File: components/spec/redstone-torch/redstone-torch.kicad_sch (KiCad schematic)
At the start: 3 parts, among them Q12 Q_NMOS_DGS

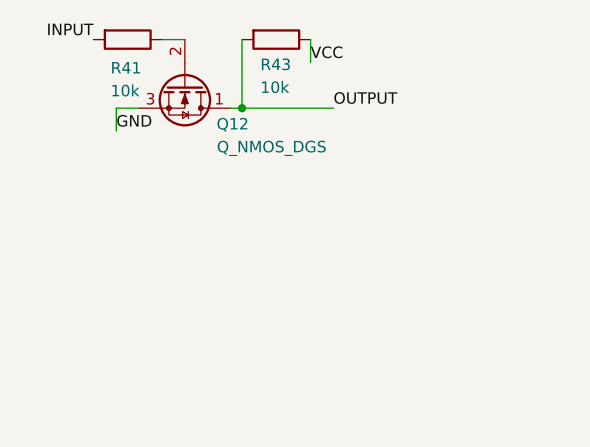
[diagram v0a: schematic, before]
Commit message: Change MOSFETs to NPN
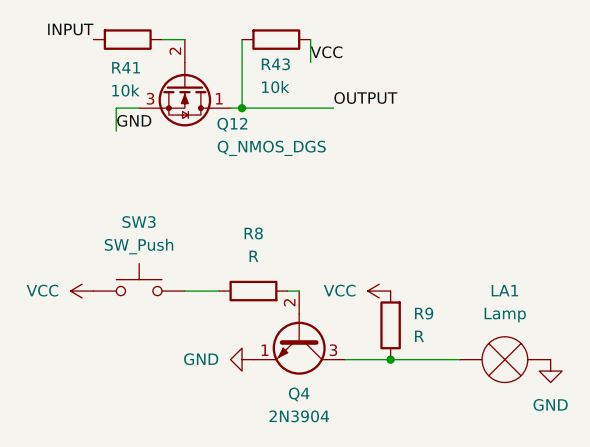
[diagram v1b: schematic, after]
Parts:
- added LA1: Lamp, symbol Device:Lamp
- added Q4: 2N3904, Package_TO_SOT_THT:TO-92_Inline, symbol Transistor_BJT:2N3904
- added R8, R9: R, symbol Device:R
- added SW3: SW_Push, symbol Switch:SW_Push
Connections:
- net GND: now also LA1.1 (-), Q4.1 (E)
- net VCC: now also R9.2, SW3.1
- new net: LA1.2 (+), Q4.3 (C), R9.1
- new net: R8.1, SW3.2
- new net: Q4.2 (B), R8.2
